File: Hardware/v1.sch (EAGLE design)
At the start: 82 parts, among them IC1 LM324D, IC2 m328p, IC3 REG1117, J1 22-27-2061-06, J2 22-27-2021-02, J3 22-27-2021-02, J4 22-27-2031-03, J5 22-27-2041-04, Q1 BSS123, Q2 BSS123, Q3 BSS123, Q5 BSS123

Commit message: solved all from #17
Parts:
- added R30: 1k, rcl:R-EU_R0603
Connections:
- new net N$27: C1.1, IC1A.+IN, R30.2, TP4.TP
- net SENSOR0: now also R30.1; no longer C1.1, IC1A.+IN, TP4.TP
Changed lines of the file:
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@@
 <?xml version="1.0" encoding="utf-8"?>
 <!DOCTYPE eagle SYSTEM "eagle.dtd">
-<eagle version="7.2.0">
+<eagle version="6.6.0">
 <drawing>
 <settings>
@@
 <part name="GND20" library="supply1" deviceset="GND" device=""/>
 <part name="P+9" library="supply1" deviceset="VCC" device=""/>
+<part name="R30" library="rcl" deviceset="R-EU_" device="R0603" value="1k"/>
 </parts>
 <sheets>
@@
 <instance part="GND20" gate="1" x="373.38" y="109.22"/>
 <instance part="P+9" gate="VCC" x="373.38" y="139.7"/>
+<instance part="R30" gate="G$1" x="40.64" y="68.58"/>
 </instances>
 <busses>
@@
 <net name="SENSOR0" class="0">
 <segment>
-<label x="38.1" y="68.58" size="1.778" layer="95" rot="R270" xref="yes"/>
-<pinref part="IC1" gate="A" pin="+IN"/>
-<pinref part="C1" gate="G$1" pin="1"/>
-<pinref part="TP4" gate="G$1" pin="TP"/>
-<wire x1="38.1" y1="68.58" x2="48.26" y2="68.58" width="0.1524" layer="91"/>
-<wire x1="48.26" y1="68.58" x2="55.88" y2="68.58" width="0.1524" layer="91"/>
-<wire x1="48.26" y1="76.2" x2="48.26" y2="68.58" width="0.1524" layer="91"/>
-<junction x="48.26" y="68.58"/>
-<wire x1="48.26" y1="68.58" x2="48.26" y2="50.8" width="0.1524" layer="91"/>
-</segment>
-<segment>
 <wire x1="218.44" y1="223.52" x2="208.28" y2="223.52" width="0.1524" layer="91"/>
 <wire x1="208.28" y1="223.52" x2="208.28" y2="228.6" width="0.1524" layer="91"/>
@@
 <label x="220.98" y="228.6" size="1.778" layer="95" xref="yes"/>
 <pinref part="J1" gate="-2" pin="S"/>
+</segment>
+<segment>
+<pinref part="R30" gate="G$1" pin="1"/>
+<wire x1="30.48" y1="68.58" x2="35.56" y2="68.58" width="0.1524" layer="91"/>
+<label x="30.48" y="68.58" size="1.778" layer="95" rot="R270" xref="yes"/>
 </segment>
 </net>
@@
 </segment>
 </net>
+<net name="N$27" class="0">
+<segment>
+<pinref part="TP4" gate="G$1" pin="TP"/>
+<wire x1="48.26" y1="76.2" x2="48.26" y2="68.58" width="0.1524" layer="91"/>
+<pinref part="IC1" gate="A" pin="+IN"/>
+<wire x1="48.26" y1="68.58" x2="55.88" y2="68.58" width="0.1524" layer="91"/>
+<pinref part="C1" gate="G$1" pin="1"/>
+<wire x1="48.26" y1="50.8" x2="48.26" y2="68.58" width="0.1524" layer="91"/>
+<junction x="48.26" y="68.58"/>
+<pinref part="R30" gate="G$1" pin="2"/>
+<wire x1="45.72" y1="68.58" x2="48.26" y2="68.58" width="0.1524" layer="91"/>
+</segment>
+</net>

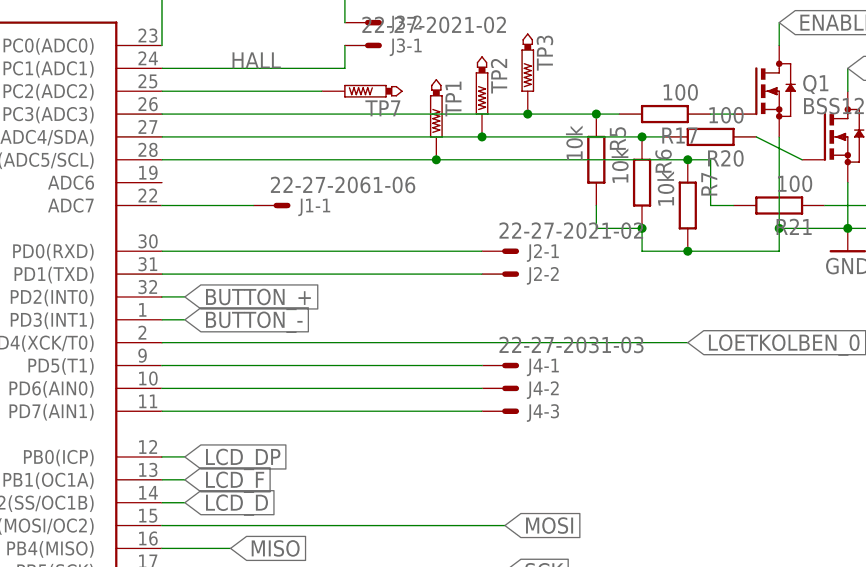
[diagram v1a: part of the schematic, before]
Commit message: Fixed issue #35 and added a third pin to make GND accessible when using UART.
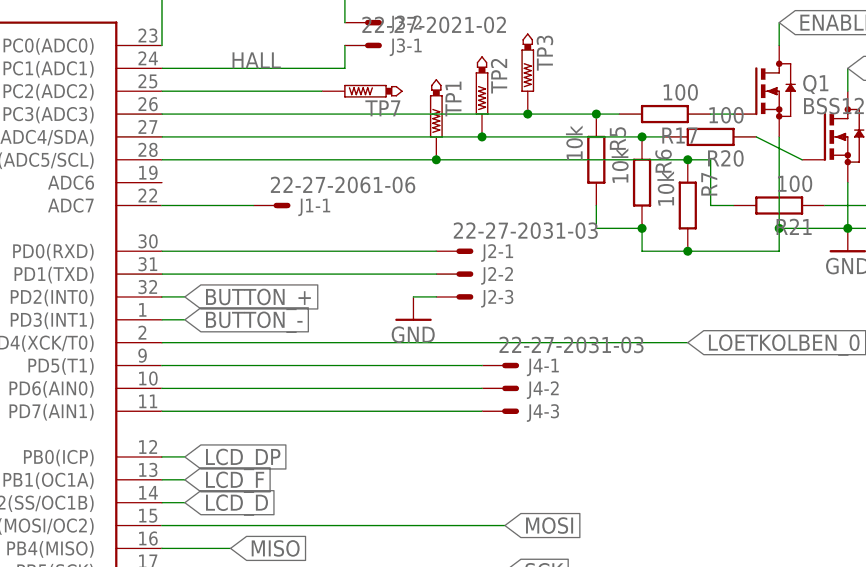
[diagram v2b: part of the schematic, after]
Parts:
- J2: value 22-27-2021-02 -> 22-27-2031-03; device con-molex:22-27-2021-02 -> con-molex:22-27-2031-03
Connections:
- net PD0 renamed N$29
- net PD1 renamed N$28
- net GND: now also J2-3.S
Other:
- moved on the sheet: J2-1, J2-2
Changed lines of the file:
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@@
 <part name="C13" library="rcl" deviceset="C-EU" device="C0603" value="100n"/>
 <part name="J5" library="con-molex" deviceset="22-?-04" device="27-2041"/>
-<part name="J2" library="con-molex" deviceset="22-?-02" device="27-2021"/>
 <part name="C14" library="rcl" deviceset="CPOL-EU" device="E3.5-8" value="330u"/>
 <part name="C16" library="rcl" deviceset="C-EU" device="C0603" value="10n"/>
@@
 <part name="P+9" library="supply1" deviceset="VCC" device=""/>
 <part name="R30" library="rcl" deviceset="R-EU_" device="R0603" value="1k"/>
+<part name="J2" library="con-molex" deviceset="22-?-03" device="27-2031"/>
+<part name="GND21" library="supply1" deviceset="GND" device=""/>
 </parts>
 <sheets>
@@
 <instance part="J5" gate="-3" x="63.5" y="223.52" rot="R90"/>
 <instance part="J5" gate="-4" x="66.04" y="223.52" rot="R90"/>
-<instance part="J2" gate="-1" x="241.3" y="147.32"/>
-<instance part="J2" gate="-2" x="241.3" y="144.78"/>
 <instance part="C14" gate="G$1" x="48.26" y="200.66"/>
 <instance part="C16" gate="G$1" x="88.9" y="60.96"/>
@@
 <instance part="P+9" gate="VCC" x="373.38" y="139.7"/>
 <instance part="R30" gate="G$1" x="40.64" y="68.58"/>
+<instance part="J2" gate="-1" x="236.22" y="147.32"/>
+<instance part="J2" gate="-2" x="236.22" y="144.78"/>
+<instance part="J2" gate="-3" x="236.22" y="142.24"/>
+<instance part="GND21" gate="1" x="231.14" y="139.7"/>
 </instances>
 <busses>
@@
 <pinref part="GND20" gate="1" pin="GND"/>
 <wire x1="373.38" y1="111.76" x2="373.38" y2="114.3" width="0.1524" layer="91"/>
+</segment>
+<segment>
+<pinref part="GND21" gate="1" pin="GND"/>
+<pinref part="J2" gate="-3" pin="S"/>
+<wire x1="233.68" y1="142.24" x2="231.14" y2="142.24" width="0.1524" layer="91"/>
 </segment>
 </net>
@@
 </segment>
 </net>
-<net name="PD0" class="0">
-<segment>
-<pinref part="IC2" gate="G$1" pin="PD0(RXD)"/>
-<wire x1="203.2" y1="147.32" x2="238.76" y2="147.32" width="0.1524" layer="91"/>
-<pinref part="J2" gate="-1" pin="S"/>
-</segment>
-</net>
-<net name="PD1" class="0">
-<segment>
-<pinref part="IC2" gate="G$1" pin="PD1(TXD)"/>
-<wire x1="238.76" y1="144.78" x2="203.2" y2="144.78" width="0.1524" layer="91"/>
-<pinref part="J2" gate="-2" pin="S"/>
-</segment>
-</net>
 <net name="PD5" class="0">
 <segment>
@@
 </segment>
 </net>
+<net name="N$28" class="0">
+<segment>
+<pinref part="IC2" gate="G$1" pin="PD1(TXD)"/>
+<pinref part="J2" gate="-2" pin="S"/>
+<wire x1="233.68" y1="144.78" x2="203.2" y2="144.78" width="0.1524" layer="91"/>
+</segment>
+</net>
+<net name="N$29" class="0">
+<segment>
+<pinref part="IC2" gate="G$1" pin="PD0(RXD)"/>
+<pinref part="J2" gate="-1" pin="S"/>
+<wire x1="233.68" y1="147.32" x2="203.2" y2="147.32" width="0.1524" layer="91"/>
+</segment>
+</net>

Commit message: Changed description in schematic from German to English.
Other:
- note added: "5V Power Supply"
- note added: "AVR n-Fets for the display"
- note added: "ISP Header"
- note added: "OpAmp for temp measurement (amp factor 431)"
- note added: "P-Fet to power the soldering iron"
- note added: "not used pads for another circuit at the lm324"
- note added: "two buttons"
- note removed: "AVR mit allen Ein- und Ausgaengen und Display-NFets"
- note removed: "For Future Use"
- note removed: "HEISSER / KAELTER"
- note removed: "OpAmp für das Thermo- element im Loetkolben Verstaerkung 431"
- note removed: "P-Fet zur Schubabschaltung am Loetkolben"
- note removed: "Programmieradapter"
- note removed: "Stromversorgung"
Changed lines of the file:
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@@
 <?xml version="1.0" encoding="utf-8"?>
 <!DOCTYPE eagle SYSTEM "eagle.dtd">
-<eagle version="6.6.0">
+<eagle version="7.2.0">
 <drawing>
 <settings>
@@
 <wire x1="320.04" y1="198.12" x2="243.84" y2="198.12" width="0.1524" layer="97"/>
 <wire x1="243.84" y1="198.12" x2="243.84" y2="261.62" width="0.1524" layer="97"/>
-<text x="246.38" y="200.66" size="3.81" layer="97">HEISSER / KAELTER</text>
-<text x="114.3" y="185.42" size="3.81" layer="97">AVR mit allen Ein- und Ausgaengen und Display-NFets</text>
-<text x="106.68" y="254" size="3.81" layer="97">P-Fet zur Schubabschaltung am Loetkolben</text>
-<text x="43.18" y="254" size="3.81" layer="97">Stromversorgung</text>
-<text x="30.48" y="127" size="3.81" layer="97">Programmieradapter</text>
-<text x="30.48" y="96.52" size="3.81" layer="97">OpAmp für das Thermo-
-element im Loetkolben
-Verstaerkung 431</text>
+<text x="246.38" y="200.66" size="3.81" layer="97">two buttons</text>
+<text x="114.3" y="185.42" size="3.81" layer="97">AVR n-Fets for the display</text>
+<text x="106.68" y="254" size="3.81" layer="97">P-Fet to power the soldering iron</text>
+<text x="43.18" y="254" size="3.81" layer="97">5V Power Supply</text>
+<text x="30.48" y="127" size="3.81" layer="97">ISP Header</text>
+<text x="30.48" y="96.52" size="3.81" layer="97">OpAmp for temp
+measurement
+(amp factor 431)</text>
 <text x="109.22" y="30.48" size="3.81" layer="97">Display 3x 7 Segment</text>
 <wire x1="325.12" y1="261.62" x2="398.78" y2="261.62" width="0.1524" layer="97"/>
@@
 <wire x1="325.12" y1="198.12" x2="325.12" y2="261.62" width="0.1524" layer="97"/>
 <wire x1="325.12" y1="198.12" x2="398.78" y2="198.12" width="0.1524" layer="97"/>
-<text x="335.28" y="254" size="3.81" layer="97">For Future Use</text>
+<text x="335.28" y="251.46" size="3.81" layer="97">not used pads for another
+circuit at the lm324</text>
 </plain>
 <instances>

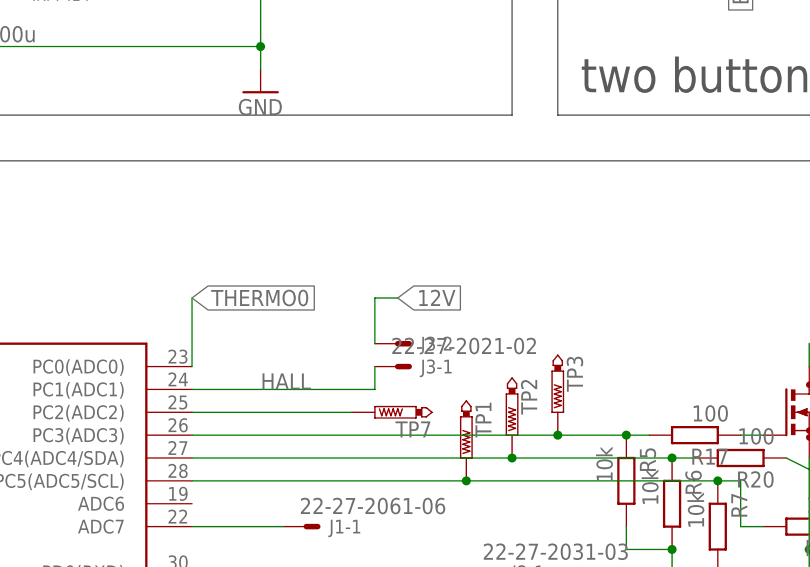
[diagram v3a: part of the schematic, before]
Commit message: fixes issue #56
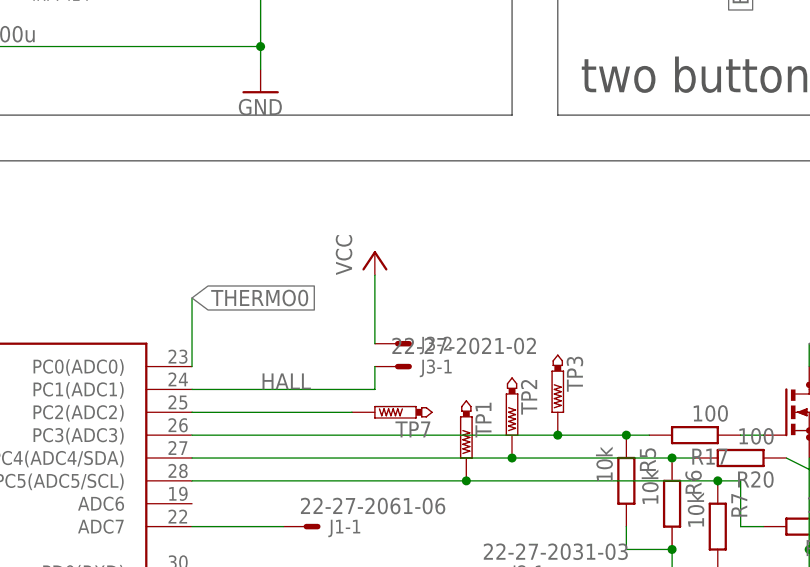
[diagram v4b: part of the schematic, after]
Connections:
- net 12V: no longer J3-2.S
- net VCC: now also J3-2.S
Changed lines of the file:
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@@
 <part name="J2" library="con-molex" deviceset="22-?-03" device="27-2031"/>
 <part name="GND21" library="supply1" deviceset="GND" device=""/>
+<part name="P+10" library="supply1" deviceset="VCC" device=""/>
 </parts>
 <sheets>
@@
 <instance part="J2" gate="-3" x="236.22" y="142.24"/>
 <instance part="GND21" gate="1" x="231.14" y="139.7"/>
+<instance part="P+10" gate="VCC" x="223.52" y="182.88"/>
 </instances>
 <busses>
@@
 <pinref part="LED2" gate="G$1" pin="A"/>
 <wire x1="373.38" y1="134.62" x2="373.38" y2="137.16" width="0.1524" layer="91"/>
+</segment>
+<segment>
+<pinref part="J3" gate="-2" pin="S"/>
+<wire x1="223.52" y1="172.72" x2="223.52" y2="180.34" width="0.1524" layer="91"/>
+<pinref part="P+10" gate="VCC" pin="VCC"/>
 </segment>
 </net>
@@
 <wire x1="180.34" y1="213.36" x2="177.8" y2="213.36" width="0.1524" layer="91"/>
 </segment>
-<segment>
-<pinref part="J3" gate="-2" pin="S"/>
-<wire x1="223.52" y1="172.72" x2="223.52" y2="177.8" width="0.1524" layer="91"/>
-<wire x1="223.52" y1="177.8" x2="226.06" y2="177.8" width="0.1524" layer="91"/>
-<label x="226.06" y="177.8" size="1.778" layer="95" xref="yes"/>
-</segment>
-</net>
+</net>

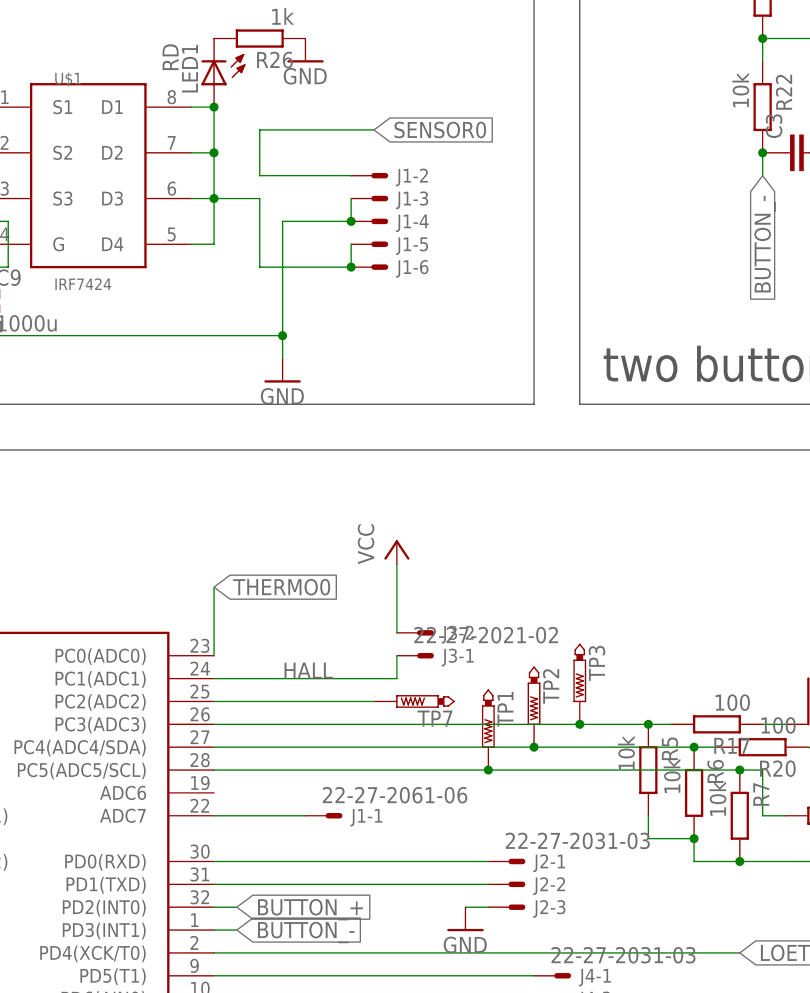
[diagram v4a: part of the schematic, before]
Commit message: - changed the 6pin header to a 7pin header to deliver 5V as well on one pin (see #60) - reduced sensor wire from 1mm to 0.8mm - rearrange wiring to compensate changes
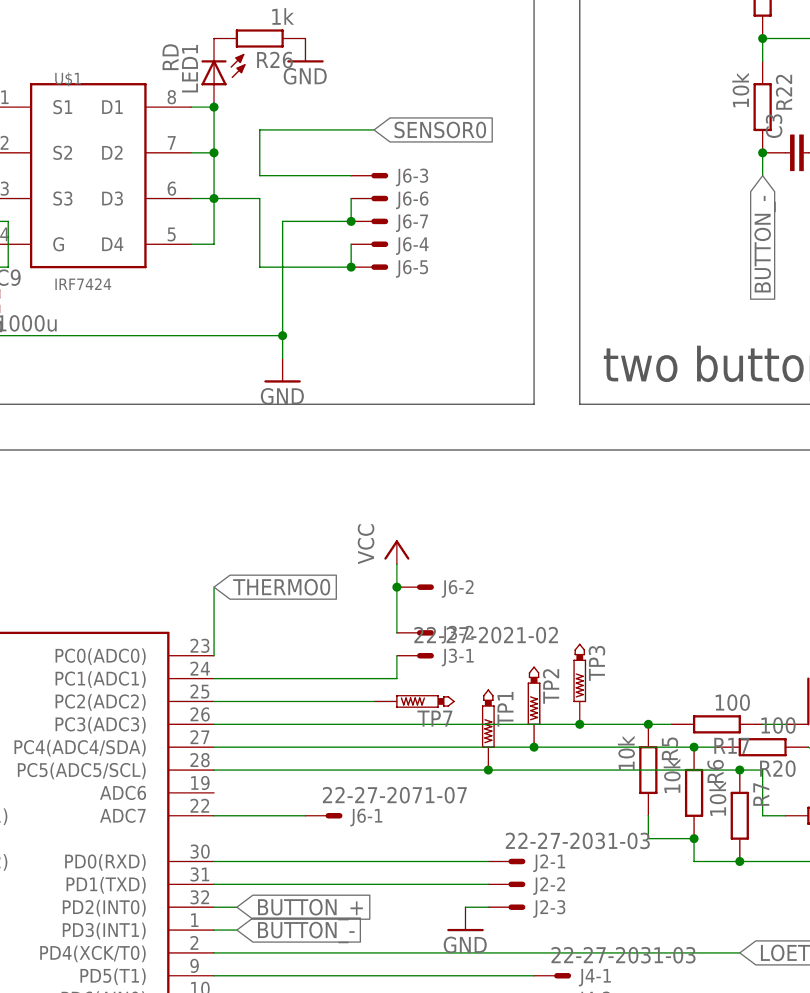
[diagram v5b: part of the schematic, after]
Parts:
- removed J1: 22-27-2061-06, con-molex:22-27-2061-06
- added J6: 22-27-2071-07, con-molex:22-27-2071-07
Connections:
- removed net ADC7: IC2.ADC7, J1-1.S
- new net STH: IC2.PC1(ADC1), J3-1.S
- net GND: now also J6-6.S, J6-7.S; no longer J1-3.S, J1-4.S
- net HALL: now also IC2.ADC7, J6-1.S; no longer IC2.PC1(ADC1), J3-1.S
- net N$33: now also J6-4.S, J6-5.S; no longer J1-5.S, J1-6.S
- net SENSOR0: now also J6-3.S; no longer J1-2.S
- net VCC: now also J6-2.S
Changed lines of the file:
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@@
 <part name="R26" library="rcl" deviceset="R-EU_" device="R0603" value="1k"/>
 <part name="GND18" library="supply1" deviceset="GND" device=""/>
-<part name="J1" library="con-molex" deviceset="22-?-06" device="27-2061"/>
 <part name="J3" library="con-molex" deviceset="22-?-02" device="27-2021"/>
 <part name="J4" library="con-molex" deviceset="22-?-03" device="27-2031"/>
@@
 <part name="GND21" library="supply1" deviceset="GND" device=""/>
 <part name="P+10" library="supply1" deviceset="VCC" device=""/>
+<part name="J6" library="con-molex" deviceset="22-?-07" device="27-2071"/>
 </parts>
 <sheets>
@@
 <instance part="R26" gate="G$1" x="208.28" y="238.76" rot="R180"/>
 <instance part="GND18" gate="1" x="213.36" y="236.22"/>
-<instance part="J1" gate="-1" x="215.9" y="152.4"/>
-<instance part="J1" gate="-2" x="220.98" y="223.52"/>
-<instance part="J1" gate="-3" x="220.98" y="220.98"/>
-<instance part="J1" gate="-4" x="220.98" y="218.44"/>
-<instance part="J1" gate="-5" x="220.98" y="215.9"/>
-<instance part="J1" gate="-6" x="220.98" y="213.36"/>
 <instance part="J3" gate="-1" x="226.06" y="170.18"/>
 <instance part="J3" gate="-2" x="226.06" y="172.72"/>
@@
 <instance part="GND21" gate="1" x="231.14" y="139.7"/>
 <instance part="P+10" gate="VCC" x="223.52" y="182.88"/>
+<instance part="J6" gate="-1" x="215.9" y="152.4"/>
+<instance part="J6" gate="-2" x="226.06" y="177.8"/>
+<instance part="J6" gate="-3" x="220.98" y="223.52"/>
+<instance part="J6" gate="-4" x="220.98" y="215.9"/>
+<instance part="J6" gate="-6" x="220.98" y="220.98"/>
+<instance part="J6" gate="-7" x="220.98" y="218.44"/>
+<instance part="J6" gate="-5" x="220.98" y="213.36"/>
 </instances>
 <busses>
@@
 <segment>
 <pinref part="J3" gate="-2" pin="S"/>
-<wire x1="223.52" y1="172.72" x2="223.52" y2="180.34" width="0.1524" layer="91"/>
+<wire x1="223.52" y1="172.72" x2="223.52" y2="177.8" width="0.1524" layer="91"/>
 <pinref part="P+10" gate="VCC" pin="VCC"/>
+<pinref part="J6" gate="-2" pin="S"/>
+<wire x1="223.52" y1="177.8" x2="223.52" y2="180.34" width="0.1524" layer="91"/>
+<junction x="223.52" y="177.8"/>
 </segment>
 </net>
@@
 <wire x1="210.82" y1="218.44" x2="218.44" y2="218.44" width="0.1524" layer="91"/>
 <wire x1="218.44" y1="220.98" x2="218.44" y2="218.44" width="0.1524" layer="91"/>
-<pinref part="J1" gate="-4" pin="S"/>
-<junction x="218.44" y="218.44"/>
-<pinref part="J1" gate="-3" pin="S"/>
 <pinref part="C9" gate="G$1" pin="-"/>
 <wire x1="177.8" y1="205.74" x2="210.82" y2="205.74" width="0.1524" layer="91"/>
@@
 <wire x1="177.8" y1="205.74" x2="172.72" y2="205.74" width="0.1524" layer="91"/>
 <junction x="177.8" y="205.74"/>
+<pinref part="J6" gate="-6" pin="S"/>
+<pinref part="J6" gate="-7" pin="S"/>
+<junction x="218.44" y="218.44"/>
 </segment>
 <segment>
@@
 <wire x1="208.28" y1="228.6" x2="220.98" y2="228.6" width="0.1524" layer="91"/>
 <label x="220.98" y="228.6" size="1.778" layer="95" xref="yes"/>
-<pinref part="J1" gate="-2" pin="S"/>
+<pinref part="J6" gate="-3" pin="S"/>
 </segment>
 <segment>
@@
 <pinref part="LED1" gate="G$1" pin="A"/>
 <junction x="203.2" y="231.14"/>
-<pinref part="J1" gate="-6" pin="S"/>
-<junction x="218.44" y="213.36"/>
-<pinref part="J1" gate="-5" pin="S"/>
 <wire x1="203.2" y1="220.98" x2="208.28" y2="220.98" width="0.1524" layer="91"/>
 <wire x1="208.28" y1="220.98" x2="208.28" y2="213.36" width="0.1524" layer="91"/>
+<pinref part="J6" gate="-4" pin="S"/>
+<pinref part="J6" gate="-5" pin="S"/>
+<junction x="218.44" y="213.36"/>
 </segment>
 </net>
@@
 </segment>
 </net>
-<net name="ADC7" class="0">
+<net name="HALL" class="0">
 <segment>
 <pinref part="IC2" gate="G$1" pin="ADC7"/>
-<pinref part="J1" gate="-1" pin="S"/>
 <wire x1="213.36" y1="152.4" x2="203.2" y2="152.4" width="0.1524" layer="91"/>
-</segment>
-</net>
-<net name="HALL" class="0">
+<pinref part="J6" gate="-1" pin="S"/>
+</segment>
+</net>
+<net name="STH" class="0">
 <segment>
 <pinref part="IC2" gate="G$1" pin="PC1(ADC1)"/>
@@
 <wire x1="203.2" y1="167.64" x2="223.52" y2="167.64" width="0.1524" layer="91"/>
 <wire x1="223.52" y1="167.64" x2="223.52" y2="170.18" width="0.1524" layer="91"/>
-<label x="210.82" y="167.64" size="1.778" layer="95"/>
-</segment>
-</net>
+</segment>
+</net>
